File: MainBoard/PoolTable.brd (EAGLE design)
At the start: 487.7 x 179.5 mm, 208 parts, among them IC1 LM317MBSTT3, IC2 LM317MBSTT3, IC3 LM317MBSTT3, IC4 93LC66SM, IC5 MIC2026-1YM, IC6 MIC2026-1YM, IC7 AP2331W-7, IC8 93LC66SM, J1 USB_A_SMT_FEMALE, J2 USB_A_SMT_FEMALE, J4 SD_CARD_SOCKET, J5 USB_A_SMT_FEMALE, J6 USB_A_SMT_FEMALE, J8 SD_CARD_SOCKET, Q1 DMG1012T-7, Q2 DMG1012T-7, Q3 DMG1012T-7, Q4 DMG1012T-7, Q5 DMG1012T-7, Q6 DMG1012T-7, U1 TMP102, U2 TMP102, U3 TMP102, U4 TMP102, U5 LAN9512-JZX, U6 FSUSB42UMX, U7 LAN9512-JZX, U8 FSUSB42UMX, Y1 25MHz, Y2 25MHz

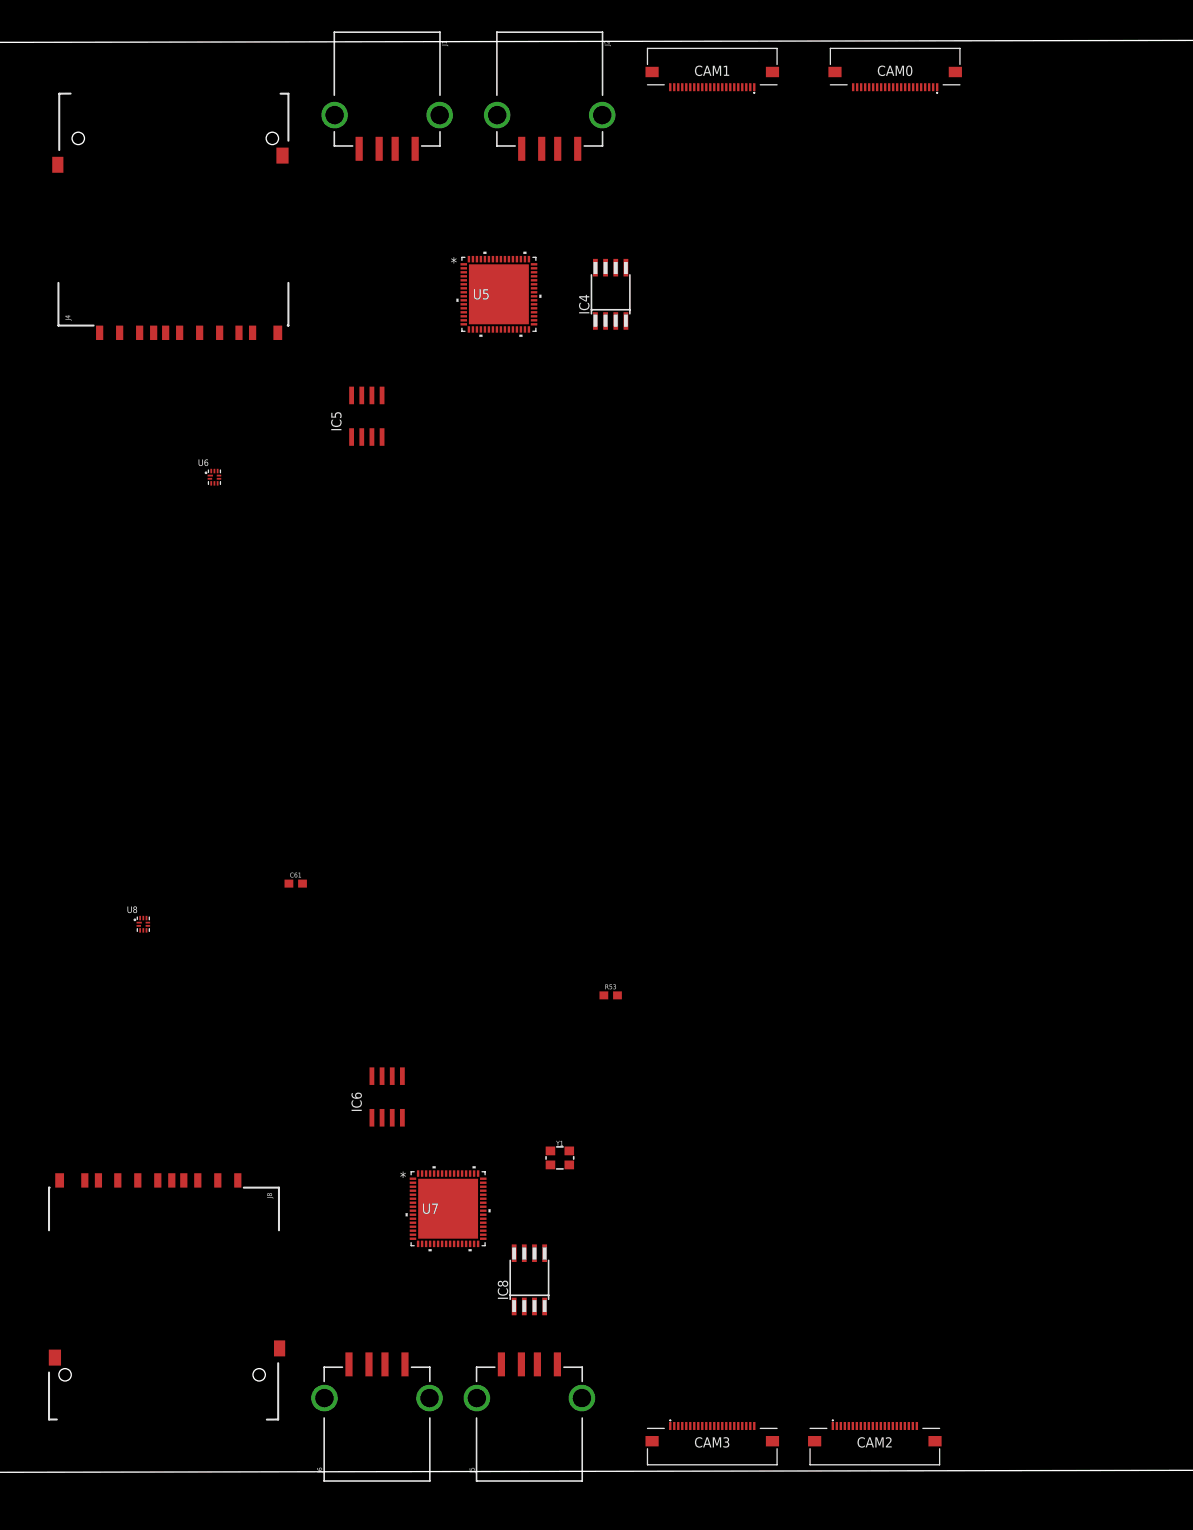
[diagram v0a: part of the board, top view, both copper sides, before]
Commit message: Updated CPU Module and removed components from Main Board
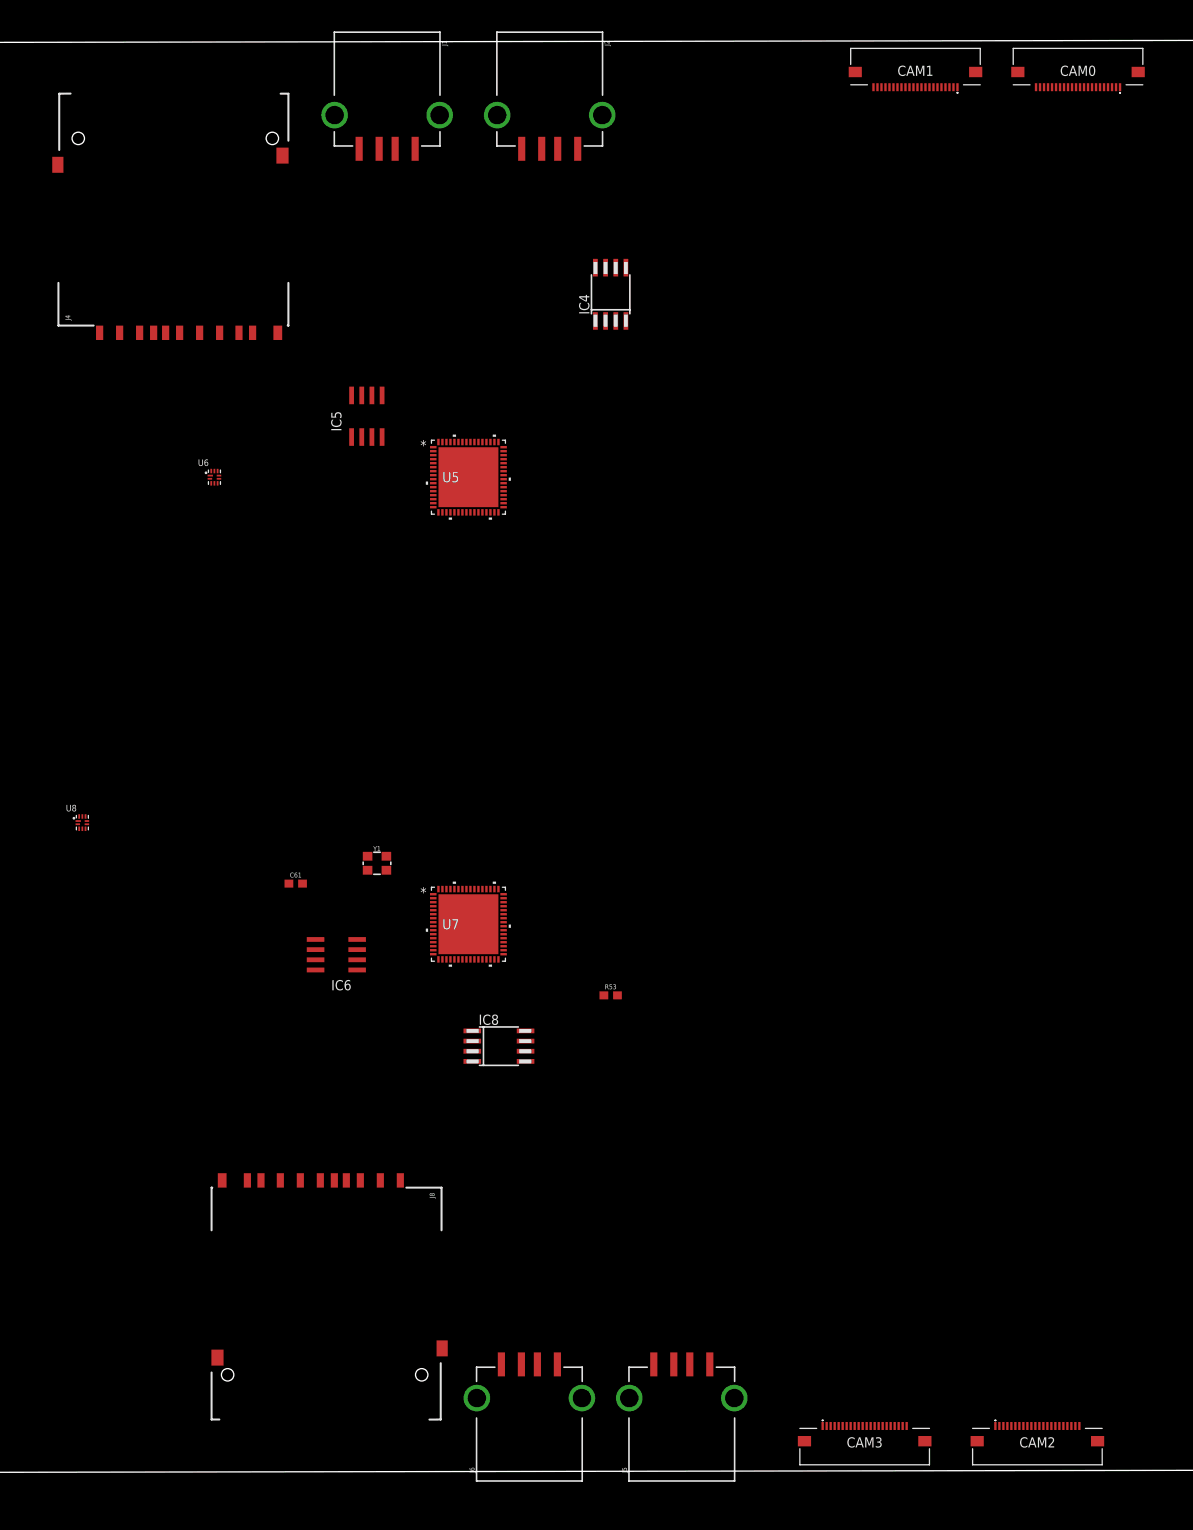
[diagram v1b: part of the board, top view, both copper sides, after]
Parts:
- moved Y1 43.3 mm to (91.4, 76.2)
- moved U7 35.7 mm to (102.9, 68.6)
- moved IC8 29.5 mm to (106.7, 53.3), turned to 270 degrees
- moved CAM1 25.4 mm to (158.8, 175.3)
- moved U5 23.2 mm to (102.9, 124.5)
- moved CAM0 22.9 mm to (179.1, 175.3)
- moved CAM2 20.3 mm to (174.0, 3.81)
- moved J8 20.3 mm to (85.1, 35.6)
- moved CAM3 19.1 mm to (152.4, 3.81)
- moved J5 19.0 mm to (129.5, 6.35)
- moved J6 19.0 mm to (110.5, 6.35)
- moved IC6 18.9 mm to (86.4, 64.8), turned to 90 degrees
- moved U8 14.8 mm to (54.6, 81.3)
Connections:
- new net CPU_CAM1_SDA: CAM3.21
- net CPU1_CAM0_SCL: now also CAM0.20
- net CPU1_CAM0_SDA: now also CAM0.21
- net CPU1_CAM1_SCL: now also CAM1.20
- net CPU1_CAM1_SDA: now also CAM1.21
- net CPU2_CAM0_SCL: now also CAM3.20
- net CPU2_CAM1_SCL: now also CAM2.20
- net CPU2_CAM1_SDA: now also CAM2.21

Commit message: Changes
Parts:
- removed C1, C4, C7: 0.1uF, rcl:C075-052X106
- removed C14, C15, C23, C24, C25, C26, C27, C28, C29, C30, C32, C33, C38, C41, C42, C44, C45, C46, C47, C48, C49, C50, C51, C52, C53, C54, C55, C57, C58: 0.1uF, SparkFun-Capacitors:0402
- removed C2, C5, C8: 1uF, resistor:085CS_1AR
- removed C3, C6, C9: 10uF, resistor:085CS_1AR
- removed C31, C34, C56, C59: 4.7uF, SparkFun-Capacitors:0402
- removed C35, C36, C60, C61: 33pF, SparkFun-Capacitors:0603
- removed C37, C43: 1.0uF, SparkFun-Capacitors:0402
- removed C39, C40: 4.7uF, SparkFun-Capacitors:0603
- removed CAM0, CAM1, CAM2, CAM3: 54548-2271, SamacSys_Parts:545482271
- removed CPU2: RPI_COMPUTE, e14_Rpi_Compute_RevC:RPI_COMPUTE
- removed D1, D2, D3, D4, D5, D6: 1N4002, diode:DO41-10
- removed D10-FULLDUPLEX, D10-FULLDUPLEX1, D11_LINK, D11_LINK1: GREEN, SparkFun-LED:LED-0603
- removed D12_FASTETHER, D12_FASTETHER1: Yellow, SparkFun-LED:LED-0603
- removed FB1, FB2, FB3, FB4: 0.05Ω/2A, SparkFun-Coils:0603
- removed IC1, IC2, IC3: LM317MBSTT3, v-reg:SOT223
- removed IC7: AP2331W-7, SamacSys_Parts:SOT95P285X130-3N
- removed J1, J2, J5, J6: USB_A_SMT_FEMALE, SparkFun-Connectors:USB-A-S-SILK-FEMALE
- removed J3, J7: (no value), SparkFun-Connectors:USB-MICROB
- removed J4, J8: SD_CARD_SOCKET, SparkFun-Connectors:SD
- removed JP1, JP2, JP3, JP4: (no value), adafruit:1X03
- removed Q1, Q2, Q3, Q4, Q5, Q6: DMG1012T-7, SamacSys_Parts:SOT50P160X80-3N
- removed R1, R3, R5: 240Ω, resistor:M0805
- removed R16, R17, R19, R41, R42, R43: 47k, SparkFun-Resistors:0603
- removed R2: 394Ω, resistor:M0805
- removed R20, R39, R40, R44: 150, SparkFun-Resistors:0603
- removed R21, R22, R23, R24, R25, R45, R46, R47, R48, R49: 100K, SparkFun-Resistors:0402
- removed R26, R28, R50, R52: 12.4K, adafruit:R0603
- removed R27, R51: 10k, SparkFun-Resistors:0603
- removed R29, R53: 1M, SparkFun-Resistors:0603
- removed R30, R54: 10K, adafruit:R0603
- removed R31, R55: 12K, adafruit:R0603
- removed R32, R33, R34, R56, R57, R58: 332R, adafruit:R0603
- removed R35, R36, R37, R38: 4.7k, SparkFun-Resistors:0603
- removed R4: 720Ω, resistor:M0805
- removed R6: 106Ω, resistor:M0805
- removed SJ1, SJ10, SJ11, SJ12, SJ13, SJ14, SJ15, SJ16, SJ17, SJ18, SJ2, SJ3, SJ4, SJ5, SJ6, SJ7, SJ8, SJ9: (no value), jumper:SJ
- removed U$4, U$5, U$6, U$7: 47uF/6.3V, SparkFun-Capacitors:0805
- removed U5, U7: LAN9512-JZX, External:QFN64_9X9MC
- removed U6, U8: FSUSB42UMX, FSUSB42UMX:IC_FSUSB42UMX
- removed Y1, Y2: 25MHz, SparkFun-Clocks:CRYSTAL-SMD-3.2X2.5MM
- added CPU0: CPU_MODULE, Modules:CPU_MODULE
- C10, C18: value 1.0uF -> 0.1uF; device SparkFun-Capacitors:0402 -> rcl:C075-052X106
- C11, C16, C19: value 0.1uF -> 1uF; device SparkFun-Capacitors:0402 -> resistor:085CS_1AR
- C12: value 4.7uF -> 10uF; device SparkFun-Capacitors:0603 -> resistor:085CS_1AR
- C13: value 4.7uF -> 0.1uF; device SparkFun-Capacitors:0603 -> rcl:C075-052X106
- C17, C20: value 0.1uF -> 10uF; device SparkFun-Capacitors:0402 -> resistor:085CS_1AR
- CPU1: value RPI_COMPUTE -> CPU_MODULE; device e14_Rpi_Compute_RevC:RPI_COMPUTE -> Modules:CPU_MODULE
- D10, D11, D12, D7, D8, D9: value GREEN -> 1N4002; device SparkFun-LED:LED-0603 -> diode:DO41-10
- IC4: value 93LC66SM -> LM317MBSTT3; device microchip:SO-08M -> v-reg:SOT223
- IC5, IC6: value MIC2026-1YM -> LM317MBSTT3; device micrel:SO08 -> v-reg:SOT223
- IC8: value 93LC66SM -> AP2331W-7; device microchip:SO-08M -> SamacSys_Parts:SOT95P285X130-3N
- R10, R7: value 4.7k -> 240Ω; device SparkFun-Resistors:0603 -> resistor:M0805
- R11: value 4.7k -> 720Ω; device SparkFun-Resistors:0603 -> resistor:M0805
- R13: value 150 -> 240Ω; device SparkFun-Resistors:0603 -> resistor:M0805
- R14: value 150 -> 106Ω; device SparkFun-Resistors:0603 -> resistor:M0805
- R8: value 4.7k -> 394Ω; device SparkFun-Resistors:0603 -> resistor:M0805
- moved C11 433.3 mm to (6.35, -5.08)
- moved C10 405.5 mm to (35.6, -24.1)
- moved C16 405.0 mm to (29.2, -5.08)
- moved C12 376.5 mm to (17.8, -5.08)
- moved R14 354.6 mm to (15.2, -54.6)
- moved D7 324.9 mm to (29.2, -31.8)
- moved C21 310.7 mm to (31.8, -52.1)
- moved C22 307.5 mm to (35.6, -52.1)
- moved C18 306.0 mm to (17.8, -33.0)
- moved R13 295.4 mm to (8.89, -54.6)
- moved C19 294.1 mm to (6.35, -14.0)
- moved C20 285.8 mm to (17.8, -14.0)
- moved R7 285.6 mm to (27.9, -47.0)
- moved R8 284.9 mm to (34.3, -47.0)
- moved D8 283.4 mm to (6.35, -39.4)
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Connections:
- removed net CPU1_CAM0_C_N: CAM0.8, CPU1.144
- removed net CPU1_CAM0_C_P: CAM0.9, CPU1.142
- removed net CPU1_CAM0_D0_N: CAM0.2, CPU1.138
- removed net CPU1_CAM0_D0_P: CAM0.3, CPU1.136
- removed net CPU1_CAM0_D1_N: CAM0.5, CPU1.150
- removed net CPU1_CAM0_D1_P: CAM0.6, CPU1.148
- removed net CPU1_CAM0_IO0: CAM0.17, SJ9.1
- removed net CPU1_CAM0_IO1: CAM0.18, SJ8.1
- removed net CPU1_CAM0_SCL: CAM0.20, SJ7.1
- removed net CPU1_CAM0_SDA: CAM0.21, SJ6.1
- removed net CPU1_CAM1_C_N: CAM1.8, CPU1.149
- removed net CPU1_CAM1_C_P: CAM1.9, CPU1.147
- removed net CPU1_CAM1_D0_N: CAM1.2, CPU1.161
- removed net CPU1_CAM1_D0_P: CAM1.3, CPU1.159
- removed net CPU1_CAM1_D1_N: CAM1.5, CPU1.155
- removed net CPU1_CAM1_D1_P: CAM1.6, CPU1.153
- removed net CPU1_CAM1_D2_N: CAM1.11, CPU1.143
- removed net CPU1_CAM1_D2_P: CAM1.12, CPU1.141
- removed net CPU1_CAM1_D3_N: CAM1.14, CPU1.137
- removed net CPU1_CAM1_D3_P: CAM1.15, CPU1.135
- removed net CPU1_CAM1_IO0: CAM1.17, SJ5.1
- removed net CPU1_CAM1_IO1: CAM1.18, SJ4.1
- removed net CPU1_CAM1_SCL: CAM1.20, SJ3.1
- removed net CPU1_CAM1_SDA: CAM1.21, SJ2.1
- removed net CPU1_EMMC_DISABLE_N: CPU1.2, Q2.3
- removed net CPU1_EMMC_EN_N_1V8: CPU1.90, Q3.1, R21.2
- removed net CPU1_ETH_18ETHPLL: C17.2, FB1.1, U5.48
- removed net CPU1_ETH_18USBPLL: C18.2, FB1.2, U5.62
- removed net CPU1_ETH_EECLK: IC4.2, U5.23
- removed net CPU1_ETH_EECS: IC4.1, R27.1, U5.24
- removed net CPU1_ETH_EEDI: IC4.4, U5.26
- removed net CPU1_ETH_EEDO: IC4.3, U5.25
- removed net CPU1_ETH_PWR1: D11.A, IC6.8, J6.VBUS, U$6.1
- removed net CPU1_ETH_PWR2: D8.A, IC5.8, J2.VBUS, U$4.1
- removed net CPU1_ETH_PWR3: D7.A, IC5.5, J1.VBUS, U$5.1
- removed net CPU1_ETH_PWR4: D10.A, IC6.5, J5.VBUS, U$7.1
- removed net CPU1_ETH_RXN: U5.53
- removed net CPU1_ETH_RXP: U5.52
- removed net CPU1_ETH_TXN: U5.56
- removed net CPU1_ETH_TXP: U5.55
- removed net CPU1_ETH_USBDM: U5.58, U6.4
- removed net CPU1_ETH_USBDP: U5.59, U6.5
- removed net CPU1_ETH_USB_DM2: J2.D-, U5.1
- removed net CPU1_ETH_USB_DM3: J1.D-, U5.3
- removed net CPU1_ETH_USB_DP2: J2.D+, U5.2
- removed net CPU1_ETH_USB_DP3: J1.D+, U5.4
- removed net CPU1_ETH_VDD18CORE: C32.2, C33.2, C34.2, U5.15, U5.38
- removed net CPU1_ETH_VDD3A: C19.2, C20.2, C21.2, C22.2, C23.2, C24.2, C25.2, FB2.2, U5.10, U5.49, U5.5, U5.51, U5.54, U5.57, U5.64
- removed net CPU1_GPIO0: CPU1.3, R8.1, SJ2.2
- removed net CPU1_GPIO1: CPU1.5, R7.1, SJ3.2
- removed net CPU1_GPIO12: CPU1.45
- removed net CPU1_GPIO13: CPU1.47
- removed net CPU1_GPIO14: CPU1.51
- removed net CPU1_GPIO15: CPU1.53
- removed net CPU1_GPIO16: CPU1.57
- removed net CPU1_GPIO17: CPU1.59
- removed net CPU1_GPIO18: CPU1.63
- removed net CPU1_GPIO22: CPU1.75
- removed net CPU1_GPIO23: CPU1.77
- removed net CPU1_GPIO24: CPU1.81
- removed net CPU1_GPIO25: CPU1.83
- removed net CPU1_GPIO26: CPU1.87
- removed net CPU1_GPIO27: CPU1.89
- removed net CPU1_GPIO28: CPU1.28, R22.1, SJ6.2
- removed net CPU1_GPIO29: CPU1.30, R23.1, SJ7.2
- removed net CPU1_GPIO30: CPU1.34, SJ8.2
- removed net CPU1_GPIO31: CPU1.36, SJ9.2
- removed net CPU1_GPIO32: CPU1.46
- removed net CPU1_GPIO33: CPU1.48
- removed net CPU1_GPIO34: CPU1.52
- removed net CPU1_GPIO35: CPU1.54
- removed net CPU1_GPIO36: CPU1.58
- removed net CPU1_GPIO37: CPU1.60
- removed net CPU1_GPIO38: CPU1.64
- removed net CPU1_GPIO39: CPU1.66
- removed net CPU1_GPIO4: CPU1.15, SJ4.2
- removed net CPU1_GPIO40: CPU1.70
- removed net CPU1_GPIO41: CPU1.72
- removed net CPU1_GPIO42: CPU1.76
- removed net CPU1_GPIO43: CPU1.78
- removed net CPU1_GPIO44: CPU1.82, R24.1
- removed net CPU1_GPIO45: CPU1.84, R25.1
- removed net CPU1_GPIO5: CPU1.17, SJ5.2
- removed net CPU1_GPIO6: CPU1.21
- removed net CPU1_GPIO7: CPU1.23
- removed net CPU1_GPIO8: CPU1.27
- removed net CPU1_SCL1: CPU1.11, R10.1, U$1.SCL, U$2.SCL, U$3.SCL, U1.1, U2.1, U3.1, U4.1, U4.4
- removed net CPU1_SDA1: CPU1.9, R11.1, U$1.SDA, U$2.SDA, U$3.SDA, U1.6, U2.6, U3.4, U3.6, U4.6
- removed net CPU1_SD_CLK: CPU1.10, J4.5
- removed net CPU1_SD_CMD: CPU1.12, J4.2
- removed net CPU1_SD_D0: CPU1.16, J4.7
- removed net CPU1_SD_D1: CPU1.18, J4.8
- removed net CPU1_SD_D2: CPU1.22, J4.9
- removed net CPU1_SD_D3: CPU1.24, J4.1
- removed net CPU1_SD_VREF: C13.2, CPU1.4, CPU1.6, SJ1.1
- removed net CPU1_SPI0_MISO: CPU1.29
- removed net CPU1_SPI0_MOSI: CPU1.33
- removed net CPU1_SPI0_SCLK: CPU1.35
- removed net CPU1_SPI1_MISO: CPU1.65
- removed net CPU1_SPI1_MOSI: CPU1.69
- removed net CPU1_SPI1_SCLK: CPU1.71
- removed net CPU1_USB_D_N: CPU1.167, U6.2
- removed net CPU1_USB_D_P: CPU1.165, U6.1
- removed net CPU1_VBUSB: J3.VBUS, JP1.1, Q1.1, R16.2
- removed net CPU2_CAM0_C_N: CAM3.8, CPU2.144
- removed net CPU2_CAM0_C_P: CAM3.9, CPU2.142
- removed net CPU2_CAM0_D0_N: CAM3.2, CPU2.138
- removed net CPU2_CAM0_D0_P: CAM3.3, CPU2.136
- removed net CPU2_CAM0_D1_N: CAM3.5, CPU2.150
- removed net CPU2_CAM0_D1_P: CAM3.6, CPU2.148
- removed net CPU2_CAM0_IO0: CAM3.17, SJ18.1
- removed net CPU2_CAM0_IO1: CAM3.18, SJ17.1
- removed net CPU2_CAM0_SCL: CAM3.20, SJ16.1
- removed net CPU2_CAM0_SDA: SJ15.1
- removed net CPU2_CAM1_C_N: CAM2.8, CPU2.149
- removed net CPU2_CAM1_C_P: CAM2.9, CPU2.147
- removed net CPU2_CAM1_D0_N: CAM2.2, CPU2.161
- removed net CPU2_CAM1_D0_P: CAM2.3, CPU2.159
- removed net CPU2_CAM1_D1_N: CAM2.5, CPU2.155
- removed net CPU2_CAM1_D1_P: CAM2.6, CPU2.153
- removed net CPU2_CAM1_D2_N: CAM2.11, CPU2.143
- removed net CPU2_CAM1_D2_P: CAM2.12, CPU2.141
- removed net CPU2_CAM1_D3_N: CAM2.14, CPU2.137
- removed net CPU2_CAM1_D3_P: CAM2.15, CPU2.135
- removed net CPU2_CAM1_IO0: CAM2.17, SJ14.1
- removed net CPU2_CAM1_IO1: CAM2.18, SJ13.1
- removed net CPU2_CAM1_SCL: CAM2.20, SJ12.1
- removed net CPU2_CAM1_SDA: CAM2.21, SJ11.1
- removed net CPU2_EMMC_DISABLE_N: CPU2.2, Q5.3
- removed net CPU2_EMMC_EN_N_1V8: CPU2.90, Q6.1, R45.2
- removed net CPU2_ETH_18ETHPLL: C42.2, FB3.1, U7.48
- removed net CPU2_ETH_18USBPLL: C43.2, FB3.2, U7.62
- removed net CPU2_ETH_EECLK: IC8.2, U7.23
- removed net CPU2_ETH_EECS: IC8.1, R51.1, U7.24
- removed net CPU2_ETH_EEDI: IC8.4, U7.26
- removed net CPU2_ETH_EEDO: IC8.3, U7.25
- removed net CPU2_ETH_RXN: U7.53
- removed net CPU2_ETH_RXP: U7.52
- removed net CPU2_ETH_TXN: U7.56
- removed net CPU2_ETH_TXP: U7.55
- removed net CPU2_ETH_USBDM: U7.58, U8.4
- removed net CPU2_ETH_USBDP: U7.59, U8.5
- removed net CPU2_ETH_USB_DM2: J6.D-, U7.1
- removed net CPU2_ETH_USB_DM3: J5.D-, U7.3
- removed net CPU2_ETH_USB_DP2: J6.D+, U7.2
- removed net CPU2_ETH_USB_DP3: J5.D+, U7.4
- removed net CPU2_ETH_VDD18CORE: C57.2, C58.2, C59.2, U7.15, U7.38
- removed net CPU2_ETH_VDD3A: C44.2, C45.2, C46.2, C47.2, C48.2, C49.2, C50.2, FB4.2, U7.10, U7.49, U7.5, U7.51, U7.54, U7.57, U7.64
- removed net CPU2_GPIO0: CPU2.3, R36.1, SJ11.2
- removed net CPU2_GPIO1: CPU2.5, R35.1, SJ12.2
- removed net CPU2_GPIO12: CPU2.45
- removed net CPU2_GPIO13: CPU2.47
- removed net CPU2_GPIO14: CPU2.51
- removed net CPU2_GPIO15: CPU2.53
- removed net CPU2_GPIO16: CPU2.57
- removed net CPU2_GPIO17: CPU2.59
- removed net CPU2_GPIO18: CPU2.63
- removed net CPU2_GPIO22: CPU2.75
- removed net CPU2_GPIO23: CPU2.77
- removed net CPU2_GPIO24: CPU2.81
- removed net CPU2_GPIO25: CPU2.83
- removed net CPU2_GPIO26: CPU2.87
- removed net CPU2_GPIO27: CPU2.89
- removed net CPU2_GPIO28: CPU2.28, R46.1, SJ15.2
- removed net CPU2_GPIO29: CPU2.30, R47.1, SJ16.2
- removed net CPU2_GPIO30: CPU2.34, SJ17.2
- removed net CPU2_GPIO31: CPU2.36, SJ18.2
- removed net CPU2_GPIO32: CPU2.46
- removed net CPU2_GPIO33: CPU2.48
- removed net CPU2_GPIO34: CPU2.52
- removed net CPU2_GPIO35: CPU2.54
- removed net CPU2_GPIO36: CPU2.58
- removed net CPU2_GPIO37: CPU2.60
- removed net CPU2_GPIO38: CPU2.64
- removed net CPU2_GPIO39: CPU2.66
- removed net CPU2_GPIO4: CPU2.15, SJ13.2
- removed net CPU2_GPIO40: CPU2.70
- removed net CPU2_GPIO41: CPU2.72
- removed net CPU2_GPIO42: CPU2.76
- removed net CPU2_GPIO43: CPU2.78
- removed net CPU2_GPIO44: CPU2.82, R48.1
- removed net CPU2_GPIO45: CPU2.84, R49.1
- removed net CPU2_GPIO5: CPU2.17, SJ14.2
- removed net CPU2_GPIO6: CPU2.21
- removed net CPU2_GPIO7: CPU2.23
- removed net CPU2_GPIO8: CPU2.27
- removed net CPU2_SCL1: CPU2.11, R37.1
- removed net CPU2_SDA1: CPU2.9, R38.1
- removed net CPU2_SD_CLK: CPU2.10, J8.5
- removed net CPU2_SD_CMD: CPU2.12, J8.2
- removed net CPU2_SD_D0: CPU2.16, J8.7
- removed net CPU2_SD_D1: CPU2.18, J8.8
- removed net CPU2_SD_D2: CPU2.22, J8.9
- removed net CPU2_SD_D3: CPU2.24, J8.1
- removed net CPU2_SD_VREF: C40.2, CPU2.4, CPU2.6, SJ10.1
- removed net CPU2_SPI0_MISO: CPU2.29
- removed net CPU2_SPI0_MOSI: CPU2.33
- removed net CPU2_SPI0_SCLK: CPU2.35
- removed net CPU2_SPI1_MISO: CPU2.65
- removed net CPU2_SPI1_MOSI: CPU2.69
- removed net CPU2_SPI1_SCLK: CPU2.71
- removed net CPU2_USB_D_N: CPU2.167, U8.2
- removed net CPU2_USB_D_P: CPU2.165, U8.1
- removed net CPU2_VBUSB: J7.VBUS, JP3.1, Q4.1, R41.2
- removed net CPU_CAM1_SDA: CAM3.21
- removed net N$1: C3.+, D2.A, IC2.1, R1.1, R2.2
- removed net N$10: IC5.1, IC5.2, U5.14
- removed net N$11: IC5.3, IC5.4, U5.16
- removed net N$13: R30.2, U5.41
- removed net N$14: JP2.2, R30.1
- removed net N$16: D8.C, R13.2
- removed net N$17: D7.C, R14.2
- removed net N$18: J3.D+, U6.7
- removed net N$19: Q1.2, R17.1, U6.10
- removed net N$2: C6.+, D4.A, IC3.1, R3.1, R4.2
- removed net N$20: J3.D-, U6.6
- removed net N$21: JP1.2, Q2.1, R19.2
- removed net N$22: D9.C, Q2.2, Q3.3
- removed net N$23: D9.A, R20.1
- removed net N$24: R31.2, U5.63
- removed net N$25: D12_FASTETHER.C, R33.2
- removed net N$26: D10-FULLDUPLEX.C, R32.2
- removed net N$27: D11_LINK.C, R34.2
- removed net N$28: R32.1, U5.20
- removed net N$29: R34.1, U5.21
- removed net N$3: C9.+, D6.A, IC1.1, R5.1, R6.2
- removed net N$30: R33.1, U5.22
- removed net N$31: IC6.1, IC6.2, U7.14
- removed net N$32: IC6.3, IC6.4, U7.16
- removed net N$33: D11.C, R39.2
- removed net N$34: D10.C, R40.2
- removed net N$35: Q4.2, R42.1, U8.10
- removed net N$36: J7.D+, U8.7
- removed net N$37: J7.D-, U8.6
- removed net N$38: JP3.2, Q5.1, R43.2
- removed net N$39: D12.C, Q5.2, Q6.3
- removed net N$40: D12.A, R44.1
- removed net N$41: R50.2, U7.50
- removed net N$42: R52.2, U7.11
- removed net N$43: C60.1, R53.1, U7.61, Y1.1
- removed net N$44: C61.1, R53.2, U7.60, Y1.3
- removed net N$45: R54.2, U7.41
- removed net N$46: JP4.2, R54.1
- removed net N$47: R55.2, U7.63
- removed net N$48: D10-FULLDUPLEX1.C, R56.2
- removed net N$49: D12_FASTETHER1.C, R57.2
- removed net N$50: D11_LINK1.C, R58.2
- removed net N$51: R56.1, U7.20
- removed net N$52: R58.1, U7.21
- removed net N$53: R57.1, U7.22
- removed net N$8: C36.1, R29.2, U5.60, Y2.3
- removed net NRESET: U5.12, U7.12
- new net CPU0_SCL0: CPU0.15, U$1.SCL, U$2.SCL, U$3.SCL, U1.1, U2.1, U3.1, U4.1, U4.4
- new net CPU0_SDA0: CPU0.13, U$1.SDA, U$2.SDA, U$3.SDA, U1.6, U2.6, U3.4, U3.6, U4.6
- net 1.8V: now also C19.+, CPU0.19, CPU1.19, D11.A, D12.C, IC6.4, R13.2; no longer C8.+, CPU1.183, CPU1.184, CPU1.185, CPU1.186, CPU2.183, CPU2.184, CPU2.185, CPU2.186, D5.A, D6.C, IC1.4, R21.1, R45.1, R5.2
- net 12V: now also C10.1, C13.1, C18.1, D11.C, D7.C, D9.C, IC4.3, IC5.3, IC6.3; no longer C1.1, C4.1, C7.1, D1.C, D3.C, D5.C, IC1.3, IC2.3, IC3.3
- net 3.3V: now also C11.+, CPU0.20, CPU1.20, D7.A, D8.C, IC4.4, R7.2; no longer C11.2, C12.1, C16.1, C2.+, C26.2, C27.2, C28.2, C29.2, C30.2, C31.2, C38.2, C39.1, C41.1, C51.2, C52.2, C53.2, C54.2, C55.2, C56.2, CAM0.22, CAM1.22, CAM2.22, CAM3.22, CPU1.189, CPU1.190, CPU1.191, CPU1.192, CPU1.193, CPU1.194, CPU1.39, CPU1.40, CPU1.41, CPU1.42, CPU2.189, CPU2.190, CPU2.191, CPU2.192, CPU2.193, CPU2.194, CPU2.39, CPU2.40, CPU2.41, CPU2.42, D1.A, D10-FULLDUPLEX.A, D10-FULLDUPLEX1.A, D11_LINK.A, D11_LINK1.A, D12_FASTETHER.A, D12_FASTETHER1.A, D2.C, FB2.1, FB4.1, IC2.4, IC4.8, IC8.8, J4.4, J8.4, JP2.1, JP4.1, R1.2, R17.2, R20.2, R28.1, R42.2, R44.2, R52.1, SJ1.2, SJ10.2, U5.19, U5.27, U5.33, U5.39, U5.40, U5.46, U6.9, U7.19, U7.27, U7.33, U7.39, U7.40, U7.46, U8.9
- net 5V: now also C16.+, C21.2, CPU0.18, CPU1.18, D10.C, D9.A, IC5.4, IC8.3; no longer C10.2, C14.2, C37.2, C5.+, CPU1.197, CPU1.198, CPU1.199, CPU1.200, CPU2.197, CPU2.198, CPU2.199, CPU2.200, D3.A, D4.C, IC3.4, IC5.7, IC6.7, IC7.3, R11.2, R3.2, R35.2, R36.2, R37.2, R38.2, R7.2, R8.2
- net GND: now also C10.2, C11.-, C12.-, C13.2, C16.-, C17.-, C18.2, C19.-, C20.-, C22.2, CPU0.1, CPU0.10, CPU0.11, CPU0.14, CPU0.17, CPU0.2, CPU0.21, CPU0.24, CPU0.27, CPU0.3, CPU0.30, CPU0.33, CPU0.37, CPU0.6, CPU0.7, CPU1.10, CPU1.11, CPU1.17, CPU1.2, CPU1.21, CPU1.24, CPU1.27, CPU1.3, CPU1.30, CPU1.33, CPU1.6, IC8.1, R11.1, R8.1; no longer C1.2, C10.1, C11.1, C12.2, C13.1, C14.1, C15.2, C16.2, C17.1, C18.1, C19.1, C2.-, C20.1, C22.1, C23.1, C24.1, C25.1, C26.1, C27.1, C28.1, C29.1, C3.-, C30.1, C31.1, C32.1, C33.1, C34.1, C35.2, C36.2, C37.1, C38.1, C39.2, C4.2, C40.1, C41.2, C42.1, C43.1, C44.1, C45.1, C46.1, C47.1, C48.1, C49.1, C5.-, C50.1, C51.1, C52.1, C53.1, C54.1, C55.1, C56.1, C57.1, C58.1, C59.1, C6.-, C60.2, C61.2, C7.2, C8.-, C9.-, CAM0.1, CAM0.10, CAM0.13, CAM0.16, CAM0.19, CAM0.23, CAM0.24, CAM0.4, CAM0.7, CAM1.1, CAM1.10, CAM1.13, CAM1.16, CAM1.19, CAM1.23, CAM1.24, CAM1.4, CAM1.7, CAM2.1, CAM2.10, CAM2.13, CAM2.16, CAM2.19, CAM2.23, CAM2.24, CAM2.4, CAM2.7, CAM3.1, CAM3.10, CAM3.13, CAM3.16, CAM3.19, CAM3.23, CAM3.24, CAM3.4, CAM3.7, CPU1.103, CPU1.104, CPU1.109, CPU1.110, CPU1.115, CPU1.116, CPU1.121, CPU1.122, CPU1.127, CPU1.13, CPU1.133, CPU1.134, CPU1.139, CPU1.140, CPU1.145, CPU1.146, CPU1.151, CPU1.152, CPU1.157, CPU1.163, CPU1.164, CPU1.169, CPU1.170, CPU1.181, CPU1.182, CPU1.187, CPU1.188, CPU1.19, CPU1.195, CPU1.196, CPU1.20, CPU1.25, CPU1.26, CPU1.31, CPU1.32, CPU1.38, CPU1.43, CPU1.44, CPU1.49, CPU1.50, CPU1.55, CPU1.56, CPU1.61, CPU1.62, CPU1.67, CPU1.68, CPU1.73, CPU1.74, CPU1.79, CPU1.8, CPU1.80, CPU1.85, CPU1.86, CPU1.91, CPU1.92, CPU1.97, CPU1.98, CPU2.1, CPU2.103, CPU2.104, CPU2.109, CPU2.110, CPU2.115, CPU2.116, CPU2.121, CPU2.122, CPU2.127, CPU2.13, CPU2.133, CPU2.134, CPU2.139, CPU2.14, CPU2.140, CPU2.145, CPU2.146, CPU2.151, CPU2.152, CPU2.157, CPU2.163, CPU2.164, CPU2.169, CPU2.170, CPU2.181, CPU2.182, CPU2.187, CPU2.188, CPU2.19, CPU2.195, CPU2.196, CPU2.20, CPU2.25, CPU2.26, CPU2.31, CPU2.32, CPU2.37, CPU2.38, CPU2.43, CPU2.44, CPU2.49, CPU2.50, CPU2.55, CPU2.56, CPU2.61, CPU2.62, CPU2.67, CPU2.68, CPU2.7, CPU2.73, CPU2.74, CPU2.79, CPU2.8, CPU2.80, CPU2.85, CPU2.86, CPU2.91, CPU2.92, CPU2.97, CPU2.98, IC4.5, IC5.6, IC6.6, IC7.1, IC8.5, J1.GND, J1.SHLD1, J1.SHLD2, J2.GND, J2.SHLD1, J2.SHLD2, J3.GND, J3.MT1, J3.MT2, J3.P$1, J3.P$2, J4.3, J4.6, J4.SH@1, J4.SH@2, J5.GND, J5.SHLD1, J5.SHLD2, J6.GND, J6.SHLD1, J6.SHLD2, J7.GND, J7.MT1, J7.MT2, J7.P$1, J7.P$2, J8.3, J8.6, J8.SH@1, J8.SH@2, JP1.3, JP2.3, JP3.3, JP4.3, Q1.3, Q3.2, Q4.3, Q6.2, R13.1, R16.1, R19.1, R2.1, R22.2, R23.2, R24.2, R25.2, R26.1, R27.2, R31.1, R39.1, R4.1, R40.1, R41.1, R43.1, R46.2, R47.2, R48.2, R49.2, R50.1, R51.2, R55.1, R6.1, U$4.2, U$5.2, U$6.2, U$7.2, U5.34, U5.65, U6.3, U7.34, U7.65, U8.3, Y1.2, Y1.4, Y2.2, Y2.4
- net H5V: now also C22.1, IC8.2; no longer C15.1, IC7.2
- net N$4: now also C12.+, D8.A, IC4.1, R7.1, R8.2; no longer R26.2, U5.50
- net N$5: now also C17.+, D10.A, IC5.1, R10.1, R11.2; no longer R28.2, U5.11
- net N$7: now also C20.+, D12.A, IC6.1, R13.1, R14.2; no longer C35.1, R29.1, U5.61, Y2.1

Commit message: Added Connectors and Molex
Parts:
- removed C10, C13: 0.1uF, rcl:C075-052X106
- removed C11, C16: 1uF, resistor:085CS_1AR
- removed C12, C17: 10uF, resistor:085CS_1AR
- removed C21, C22: 0.1uF, SparkFun-Capacitors:0402
- removed D10, D7, D8, D9: 1N4002, diode:DO41-10
- removed IC4, IC5: LM317MBSTT3, v-reg:SOT223
- removed IC8: AP2331W-7, SamacSys_Parts:SOT95P285X130-3N
- removed R10, R7: 240Ω, resistor:M0805
- removed R11: 720Ω, resistor:M0805
- removed R8: 394Ω, resistor:M0805
- removed U$1, U$2, U$3: PWM_MODULE, Modules:PWM_MODULE
- added LED0, LED1, LED2: MOLEX-ULTRAFIT-1X04VERT, External:MOLEX-ULTRAFIT-1X04V
- added M0, M1, M2, M3, M4, M5, M6, M7, M8, S0, S1, S2, S3, S4: MOLEX-ULTRAFIT-1X03VERT, External:MOLEX-ULTRAFIT-1X03V
- added PWM0, PWM1, PWM2: PWM_MODULE, Modules:PWM_MODULE
- added PWR_IN: MOLEX-ULTRAFIT-1X08, External:MOLEX-ULTRAFIT-1X08
- added REG0: 5V, External:POLOLU-REG
- added REG1: 3.3V, External:POLOLU-REG
- moved R15 289.8 mm to (31.8, 18.5), turned to 180 degrees
- moved U4 289.2 mm to (35.6, 19.1)
- moved R9 225.0 mm to (94.4, 82.0), turned to 180 degrees
- moved U1 216.2 mm to (99.1, 82.5)
- moved D11 214.2 mm to (189.9, 63.5), turned to 90 degrees
- moved R14 204.0 mm to (186.7, 55.9), turned to 180 degrees
- moved R13 200.3 mm to (178.1, 52.6), turned to 270 degrees
- moved D12 199.7 mm to (185.4, 63.5), turned to 270 degrees
- moved C19 189.1 mm to (176.5, 68.6)
- moved C18 187.4 mm to (185.4, 50.8)
- moved IC6 181.2 mm to (180.3, 59.7)
- moved CPU1 177.8 mm to (68.6, 87.6)
- moved C20 171.0 mm to (172.7, 58.4), turned to 270 degrees
- moved R18 151.4 mm to (189.7, 21.3), turned to 270 degrees
- moved U2 144.6 mm to (190.5, 25.4)
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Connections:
- removed net H5V: C22.1, IC8.2
- removed net N$4: C12.+, D8.A, IC4.1, R7.1, R8.2
- removed net N$5: C17.+, D10.A, IC5.1, R10.1, R11.2
- net 12V: now also PWR_IN.P$1, PWR_IN.P$2, PWR_IN.P$3, PWR_IN.P$4, REG0.P$1, REG0.P$14, REG0.P$15, REG1.P$1, REG1.P$14, REG1.P$15; no longer C10.1, C13.1, D7.C, D9.C, IC4.3, IC5.3
- net 3.3V: now also REG1.P$4, REG1.P$7, REG1.P$8; no longer C11.+, D7.A, D8.C, IC4.4, R7.2
- net 5V: now also M0.P$2, M1.P$2, M2.P$2, M3.P$2, M4.P$2, M5.P$2, M6.P$2, M7.P$2, M8.P$2, PWM0.5V, PWM1.5V, PWM2.5V, REG0.P$4, REG0.P$7, REG0.P$8, S0.P$2, S1.P$2, S2.P$2, S3.P$2, S4.P$2; no longer C16.+, C21.2, D10.C, D9.A, IC5.4, IC8.3, R10.2, U$1.5V, U$2.5V, U$3.5V
- net CPU0_SCL0: now also PWM0.SCL, PWM1.SCL, PWM2.SCL; no longer U$1.SCL, U$2.SCL, U$3.SCL
- net CPU0_SDA0: now also PWM0.SDA, PWM1.SDA, PWM2.SDA; no longer U$1.SDA, U$2.SDA, U$3.SDA
- net GND: now also M0.P$1, M1.P$1, M2.P$1, M3.P$1, M4.P$1, M5.P$1, M6.P$1, M7.P$1, M8.P$1, PWM0.GND, PWM1.GND, PWM2.GND, PWR_IN.P$5, PWR_IN.P$6, PWR_IN.P$7, PWR_IN.P$8, REG0.P$11, REG0.P$12, REG0.P$16, REG0.P$17, REG0.P$2, REG0.P$3, REG0.P$5, REG0.P$6, REG1.P$11, REG1.P$12, REG1.P$16, REG1.P$17, REG1.P$2, REG1.P$3, REG1.P$5, REG1.P$6, S0.P$1, S1.P$1, S2.P$1, S3.P$1, S4.P$1; no longer C10.2, C11.-, C12.-, C13.2, C16.-, C17.-, C21.1, C22.2, IC8.1, R11.1, R8.1, U$1.GND, U$2.GND, U$3.GND
- net PWM1_0: now also M0.P$3, PWM0.PWM0; no longer U$1.PWM0
- net PWM1_1: now also M1.P$3, PWM0.PWM1; no longer U$1.PWM1
- net PWM1_10: now also PWM0.PWM10; no longer U$1.PWM10
- net PWM1_11: now also PWM0.PWM11; no longer U$1.PWM11
- net PWM1_12: now also PWM0.PWM12; no longer U$1.PWM12
- net PWM1_13: now also PWM0.PWM13; no longer U$1.PWM13
- net PWM1_14: now also PWM0.PWM14; no longer U$1.PWM14
- net PWM1_15: now also PWM0.PWM15; no longer U$1.PWM15
- net PWM1_2: now also M2.P$3, PWM0.PWM2; no longer U$1.PWM2
- net PWM1_3: now also M3.P$3, PWM0.PWM3; no longer U$1.PWM3
- net PWM1_4: now also M4.P$3, PWM0.PWM4; no longer U$1.PWM4
- net PWM1_5: now also M5.P$3, PWM0.PWM5; no longer U$1.PWM5
- net PWM1_6: now also M6.P$3, PWM0.PWM6; no longer U$1.PWM6
- net PWM1_7: now also M7.P$3, PWM0.PWM7; no longer U$1.PWM7
- net PWM1_8: now also M8.P$3, PWM0.PWM8; no longer U$1.PWM8
- net PWM1_9: now also PWM0.PWM9; no longer U$1.PWM9
- net PWM2_0: now also PWM2.PWM0, S0.P$3; no longer U$3.PWM0
- net PWM2_1: now also PWM2.PWM1, S1.P$3; no longer U$3.PWM1
- net PWM2_10: now also PWM2.PWM10; no longer U$3.PWM10
- net PWM2_11: now also PWM2.PWM11; no longer U$3.PWM11
- net PWM2_12: now also PWM2.PWM12; no longer U$3.PWM12
- net PWM2_13: now also PWM2.PWM13; no longer U$3.PWM13
- net PWM2_14: now also PWM2.PWM14; no longer U$3.PWM14
- net PWM2_15: now also PWM2.PWM15; no longer U$3.PWM15
- net PWM2_2: now also PWM2.PWM2, S2.P$3; no longer U$3.PWM2
- net PWM2_3: now also PWM2.PWM3, S3.P$3; no longer U$3.PWM3
- net PWM2_4: now also PWM2.PWM4, S4.P$3; no longer U$3.PWM4
- net PWM2_5: now also PWM2.PWM5; no longer U$3.PWM5
- net PWM2_6: now also PWM2.PWM6; no longer U$3.PWM6
- net PWM2_7: now also PWM2.PWM7; no longer U$3.PWM7
- net PWM2_8: now also PWM2.PWM8; no longer U$3.PWM8
- net PWM2_9: now also PWM2.PWM9; no longer U$3.PWM9
- net PWM3_0: now also PWM1.PWM0; no longer U$2.PWM0
- net PWM3_1: now also PWM1.PWM1; no longer U$2.PWM1
- net PWM3_10: now also PWM1.PWM10; no longer U$2.PWM10
- net PWM3_11: now also PWM1.PWM11; no longer U$2.PWM11
- net PWM3_12: now also PWM1.PWM12; no longer U$2.PWM12
- net PWM3_13: now also PWM1.PWM13; no longer U$2.PWM13
- net PWM3_14: now also PWM1.PWM14; no longer U$2.PWM14
- net PWM3_15: now also PWM1.PWM15; no longer U$2.PWM15
- net PWM3_2: now also PWM1.PWM2; no longer U$2.PWM2
- net PWM3_3: now also PWM1.PWM3; no longer U$2.PWM3
- net PWM3_4: now also PWM1.PWM4; no longer U$2.PWM4
- net PWM3_5: now also PWM1.PWM5; no longer U$2.PWM5
- net PWM3_6: now also PWM1.PWM6; no longer U$2.PWM6
- net PWM3_7: now also PWM1.PWM7; no longer U$2.PWM7
- net PWM3_8: now also PWM1.PWM8; no longer U$2.PWM8
- net PWM3_9: now also PWM1.PWM9; no longer U$2.PWM9
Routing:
- net 12V: track 0.00 -> 136.9 mm
- net 1.8V: track 0.00 -> 32.6 mm, vias 0 -> 2
- net N$7: track 0.00 -> 21.0 mm, vias 0 -> 2
- added copper zone on layer 1, net GND
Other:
- board size 487.7 x 179.5 mm -> 212.1 x 178.3 mm
- board text added: "M0"
- board text added: "M1"
- board text added: "M2"
- board text added: "M3"
- board text added: "M4"
- board text added: "M5"
- board text added: "M6"
- board text added: "M7"
- board text added: "M8"
- board text added: "S0"
- board text added: "S1"
- board text added: "S2"
- board text added: "S3"
- board text added: "S4"
